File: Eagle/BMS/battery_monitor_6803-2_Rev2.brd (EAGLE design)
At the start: 88.1 x 53.3 mm, 65 parts, among them Q1 MOSFET-PCHANNELIRLML2244, Q10 IRF9530, Q2 MOSFET-NCHANNELBSS138, Q3 MOSFET-PCHANNELIRLML2244, Q4 MOSFET-PCHANNELIRLML2244, Q5 MOSFET-PCHANNELIRLML2244, Q6 MOSFET-NCHANNELBSS138, Q7 MOSFET-NCHANNELBSS138, Q8 MOSFET-NCHANNELBSS138, Q9 PMOS_AO4435

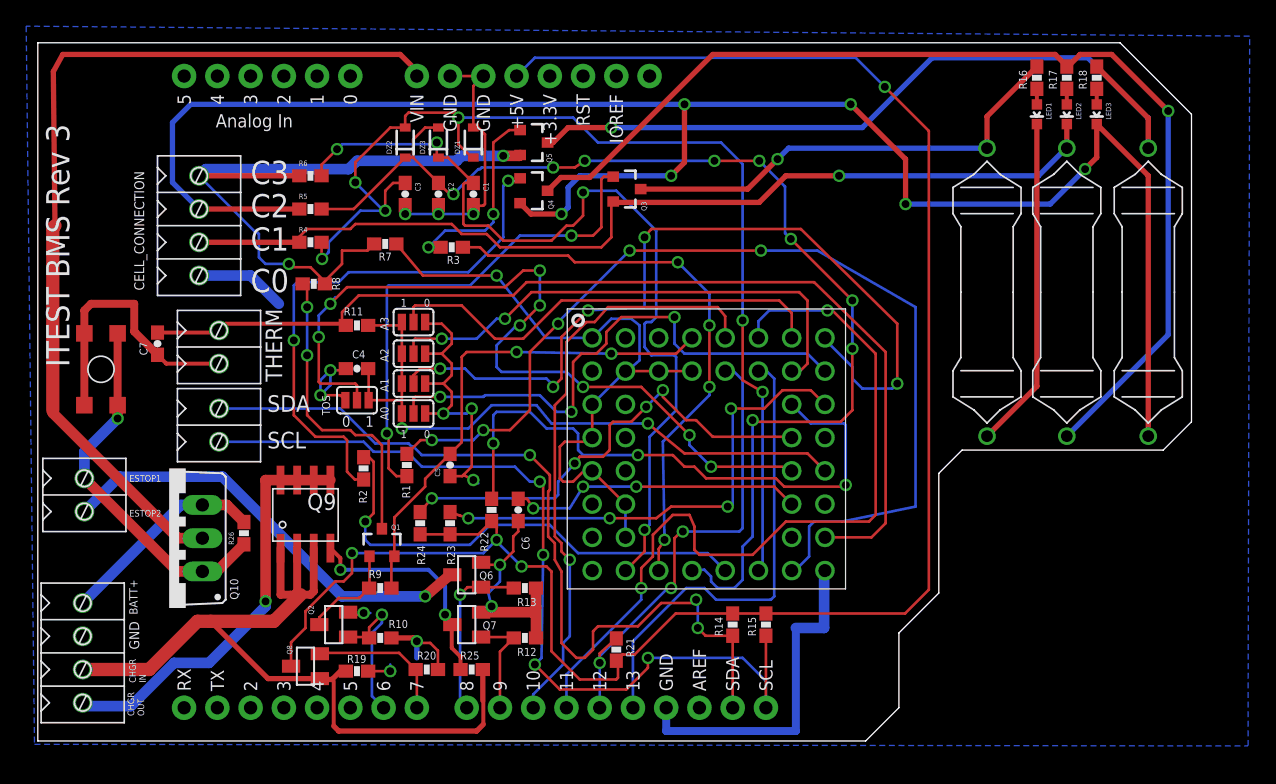
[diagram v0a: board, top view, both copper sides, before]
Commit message: Renumbered BMS revisions and wrote code for interrupt-driven encoders.
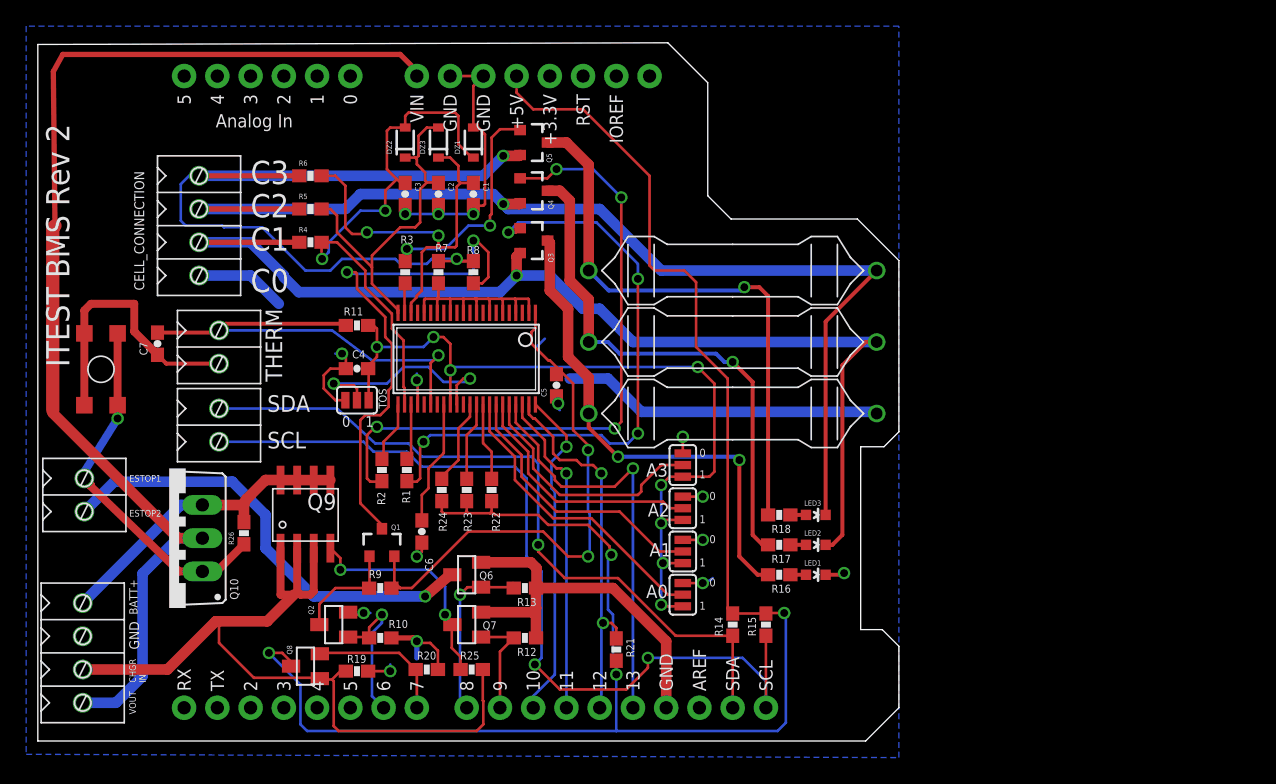
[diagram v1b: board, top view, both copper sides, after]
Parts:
- removed U$9: LTC6803, Clayton:LTC6803_BREAKOUT
- added U$5: LTC6803-2, isaac1:FSOP-44
- R26: value 1Meg -> 1MEG
- moved R16 42.8 mm to (58.2, 13.5), turned to 180 degrees
- moved R17 41.9 mm to (58.2, 15.7), turned to 180 degrees
- moved R18 41.3 mm to (58.2, 18.0), turned to 180 degrees
- moved LED1 39.0 mm to (61.0, 13.5), turned to 270 degrees
- moved LED2 38.1 mm to (61.0, 15.7), turned to 270 degrees
- moved LED3 37.4 mm to (61.0, 18.0), turned to 270 degrees
- moved U$3 31.8 mm to (54.6, 36.7), turned to 90 degrees
- moved U$2 25.8 mm to (54.6, 31.2), turned to 90 degrees
- moved A0 24.8 mm to (50.8, 11.9), turned to 90 degrees
- moved A1 24.2 mm to (50.8, 15.2), turned to 90 degrees
- moved A2 23.7 mm to (50.8, 18.5), turned to 90 degrees
- moved A3 23.3 mm to (50.8, 21.8), turned to 90 degrees
- moved U$1 21.5 mm to (54.6, 25.8), turned to 90 degrees
- moved R8 12.2 mm to (34.8, 36.6), turned to 270 degrees
- moved C5 10.2 mm to (41.1, 27.9)
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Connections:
- removed net A0: A0.2, U$9.AO
- removed net A1: A1.2, U$9.A1
- removed net A2: A2.2, U$9.A2
- removed net A3: A3.2, U$9.A3
- removed net C1: C3.1, DZ1.1, DZ2.2, R4.2, U$9.C1
- removed net C12: R7.2, U$9.C10, U$9.C11, U$9.C12, U$9.C4, U$9.C5, U$9.C6, U$9.C7, U$9.C8, U$9.C9
- removed net C2: C2.1, DZ2.1, DZ3.2, R5.2, U$9.C2
- removed net C3: C1.1, DZ3.1, R6.2, U$9.C3
- removed net CHARGER_OUT: Q9.5, Q9.6, Q9.7, Q9.8, U$4.P$4
- removed net GPIO1: R23.2, U$9.GPIO1
- removed net GPIO2: R22.2, U$9.GPIO2
- removed net S1: R1.2, U$9.S1
- removed net S2: R2.2, U$9.S2
- removed net S3: R3.2, U$9.S3
- removed net TOS: TOS.2, U$9.TOS
- removed net V+: C5.2, Q1.2, R9.2, U$9.V+
- removed net VREF: C6.2, U$9.VREF
- removed net VTEMP1: C7.2, R11.1, THERM.P$1, U$9.VTEMP1
- removed net WDTB: R24.2, U$9.WDTB
- new net N$14: C1.1, DZ3.1, R6.2, U$5.20
- new net N$15: C3.1, DZ1.1, DZ2.2, R4.2, U$5.24
- new net N$16: C2.1, DZ2.1, DZ3.2, R5.2, U$5.22
- new net N$17: R7.2, U$5.10, U$5.12, U$5.14, U$5.16, U$5.18, U$5.2, U$5.4, U$5.6, U$5.8
- new net N$19: C5.2, Q1.2, R9.2, U$5.1
- new net N$21: C7.2, R11.1, THERM.P$1, U$5.28
- new net N$24: R22.2, U$5.36
- new net N$25: R23.2, U$5.35
- new net N$27: R24.2, U$5.34
- new net N$28: A3.2, U$5.40
- new net N$30: A2.2, U$5.39
- new net N$31: A1.2, U$5.38
- new net N$32: A0.2, U$5.37
- new net N$33: TOS.2, U$5.32
- new net N$34: C6.2, U$5.30
- new net N$6: R2.2, U$5.23
- new net N$8: R1.2, U$5.25
- new net N$9: R3.2, U$5.21
- net +12: now also U$4.P$4
- net BATTERY+: now also Q9.5, Q9.6, Q9.7, Q9.8
- net GND: now also U$5.26; no longer U$9.V-
- net MISO: now also U$5.43; no longer U$9.SDO
- net MOSI: now also U$5.42; no longer U$9.SDI
- net SCK: now also U$5.41; no longer U$9.SCKI
- net SS: now also U$5.44; no longer U$9.CSBI
- net VREG: now also U$5.31; no longer U$9.VREG
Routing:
- net C2: track 88.4 -> 0.00 mm, vias 9 -> 0
- net C1: track 85.5 -> 0.00 mm, vias 6 -> 0
- net VTEMP1: track 78.7 -> 0.00 mm
- net S1: track 76.8 -> 0.00 mm, vias 5 -> 0
- net C3: track 68.2 -> 0.00 mm, vias 4 -> 0
- net A1: track 63.8 -> 0.00 mm, vias 5 -> 0
- net TOS: track 63.4 -> 0.00 mm, vias 8 -> 0
- net N$3: track 141.2 -> 84.1 mm, vias 6 -> 1
- net C12: track 52.4 -> 0.00 mm, vias 1 -> 0
- net GPIO2: track 46.1 -> 0.00 mm, vias 3 -> 0
- net S3: track 43.1 -> 0.00 mm, vias 4 -> 0
- net N$10: track 82.4 -> 40.4 mm
- net A0: track 41.8 -> 0.00 mm, vias 3 -> 0
- net N$15: track 0.00 -> 41.7 mm, vias 0 -> 2
- net N$19: track 0.00 -> 41.4 mm, vias 0 -> 2
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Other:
- board size 88.1 x 53.3 mm -> 65.8 x 53.3 mm
- board text added: "ITEST BMS Rev 2"
- board text added: "VOUT"
- board text removed: "CHGR OUT"
- board text removed: "ITEST BMS Rev 3"

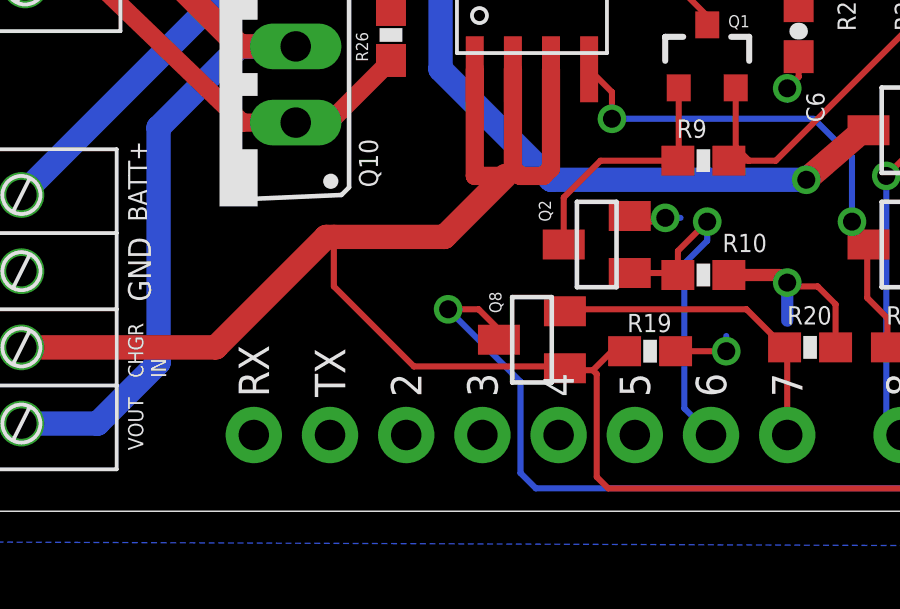
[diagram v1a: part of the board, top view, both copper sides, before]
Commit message: Fixed error with charging line shorting to +5V
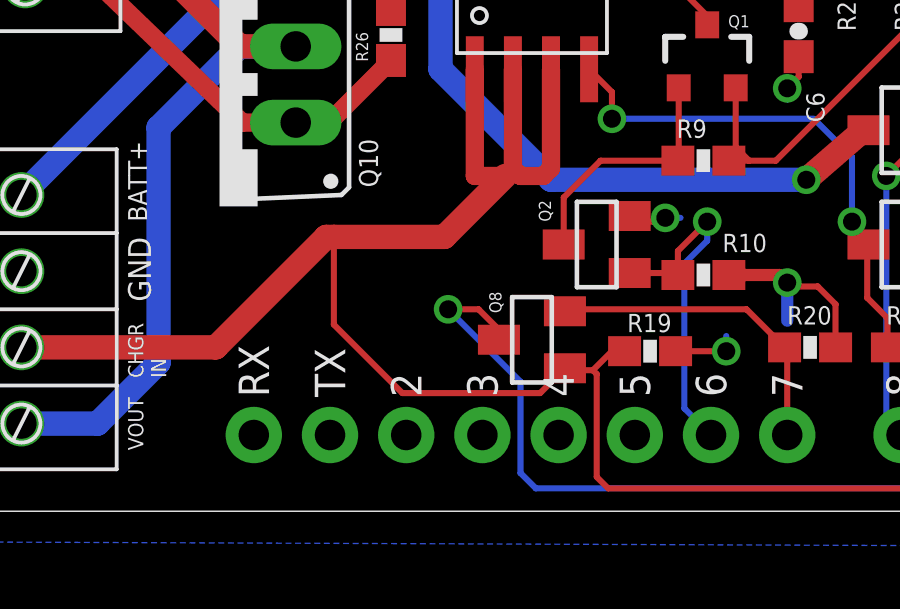
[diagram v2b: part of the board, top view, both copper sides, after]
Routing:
- net CHARGER_IN: track 63.9 -> 65.4 mm
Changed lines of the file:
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@@
 <wire x1="11.43" y1="6.223" x2="4.953" y2="6.223" width="0.8128" layer="1"/>
 <wire x1="23.071" y1="5.527" x2="23.01" y2="5.588" width="0.2032" layer="1"/>
-<wire x1="23.01" y1="5.588" x2="18.034" y2="5.588" width="0.2032" layer="1"/>
-<wire x1="18.034" y1="5.588" x2="15.367" y2="8.255" width="0.2032" layer="1"/>
-<wire x1="15.367" y1="8.255" x2="15.367" y2="9.906" width="0.2032" layer="1"/>
+<wire x1="15.367" y1="6.985" x2="15.367" y2="9.906" width="0.2032" layer="1"/>
 <wire x1="15.367" y1="9.906" x2="19.05" y2="9.906" width="0.8128" layer="1"/>
 <wire x1="19.05" y1="9.906" x2="21.082" y2="11.938" width="0.8128" layer="1"/>
+<wire x1="23.01" y1="5.588" x2="22.987" y2="5.588" width="0.4064" layer="1"/>
+<wire x1="15.367" y1="6.985" x2="17.653" y2="4.699" width="0.2032" layer="1"/>
+<wire x1="17.653" y1="4.699" x2="22.243" y2="4.699" width="0.2032" layer="1"/>
+<wire x1="22.243" y1="4.699" x2="23.071" y2="5.527" width="0.2032" layer="1"/>
 </signal>
 <signal name="N$24">
